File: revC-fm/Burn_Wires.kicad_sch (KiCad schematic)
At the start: 14 parts, among them Q19 MMBT2222AWT3G, Q20 DMN100-7-F, Q21 DMN100-7-F, Q22 IRF7404TRPBF, Q23 IRF7404TRPBF, U23 PE014006

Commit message: working revC
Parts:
- added J6 (x2): T1M-04-F-SV-L, mainboard-SLI:T1M-04-F-SV-L, symbol Connector_Generic:Conn_01x04
- Q19: value MMBT2222AWT3G -> MMBT2222LT1G; footprint Package_TO_SOT_SMD:SOT-323_SC-70 -> Package_TO_SOT_SMD:SOT-23-3
- Q20, Q21: value DMN100-7-F -> MMBT2222AWT3G; footprint mainboard:SOT-23 -> Package_TO_SOT_SMD:SOT-323_SC-70; symbol mainboard:IRLML2803TRPBF -> Device:Q_NPN_BEC; Flight DMN100-7-F -> (none)
- Q22, Q23: symbol mainboard:NDS8434 -> mainboard_SLI:IRF7404TRPBF; Flight IRF7404TRPBF -> (none)
- R167: value 4.7k -> 1k
- R168, R169: value 10k -> 1k
- R170, R171: value 4.7k -> 1Meg
- R172: value 100k -> 10Meg
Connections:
- net ENAB_BURN1: no longer R168.1
- net ENAB_BURN2: no longer R169.1
- net GND: now also J6.3 (Pin_3), J6.3 (Pin_3), J6.4 (Pin_4), J6.4 (Pin_4); no longer R168.2, R169.2
- net VBURN1: now also Q22.1 (S), Q22.2 (S), Q22.3 (S), J6.1 (Pin_1), J6.2 (Pin_2); no longer Q22.5 (Drain), Q22.6 (Drain), Q22.7 (Drain), Q22.8 (Drain)
- net VBURN2: now also J6.1 (Pin_1), J6.2 (Pin_2)
- net VBURN_A_IN: now also Q22.5 (D), Q22.6 (D), Q22.7 (D), Q22.8 (D); no longer Q22.1 (Source), Q22.2 (Source), Q22.3 (Source)
- net at Q20.3 (C), R172.1: now also R168.1; no longer Q22.4 (Gate)
- net at Q21.3 (C), R173.1: now also R169.1; no longer Q23.4 (Gate)
- new net: Q23.4 (G), R169.2
- new net: Q22.4 (G), R168.2
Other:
- note added: "in a larger package than other NPN's due to temp. derating"
- moved on the sheet: Q19, R167, R168, R169, R170, R171, R173

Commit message: working revC
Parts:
- Q20: renamed from Q22; value IRF7404TRPBF -> BSZ180P03NS3GATMA1; footprint Package_SO:SOIC-8_3.9x4.9mm_P1.27mm -> mainboard-SLI:PG-TSDSON-8_3.3x3.3mm; symbol mainboard_SLI:IRF7404TRPBF -> mainboard_SLI:BSZ180
- Q23: value IRF7404TRPBF -> BSZ180P03NS3GATMA1; footprint Package_SO:SOIC-8_3.9x4.9mm_P1.27mm -> mainboard-SLI:PG-TSDSON-8_3.3x3.3mm; symbol mainboard_SLI:IRF7404TRPBF -> mainboard_SLI:BSZ180
- renumbered D9 to D12, Q19 to Q21, Q20 to Q22, Q21 to Q24, R172 to R149, R168 to R150, R167 to R151, R170 to R152, R173 to R153, R169 to R154, R171 to R155, U23 to U20
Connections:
- net VBURN1: no longer Q20.2 (S), Q20.3 (S)
- net VBURN2: no longer Q23.6 (D), Q23.7 (D), Q23.8 (D)
- net VBURN_A_IN: no longer Q20.6 (D), Q20.7 (D), Q20.8 (D), Q23.2 (S), Q23.3 (S)

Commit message: working revC
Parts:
- removed D12: DFLS130L, mainboard:PWRDI-123, symbol mainboard:DFLS130L
- removed Q22, Q24: MMBT2222AWT3G, Package_TO_SOT_SMD:SOT-323_SC-70, symbol Device:Q_NPN_BEC
- added D9: SBRT5A50SA-13, Diode_SMD:D_SMA, symbol mainboard-rescue:D_Schottky-Device-mainboard-rescue
- added Q29 (x2): MMDT5551-7-F, Package_TO_SOT_SMD:SOT-363_SC-70-6, symbol Transistor_BJT:MMDT5551
- J6: footprint mainboard-SLI:T1M-04-F-SV-L -> SierraLobo:SAMTEC_T1M-04-F-SV-L
- K1: renamed from U20; footprint mainboard:RELAY_PE014006 -> SierraLobo:PE014006; symbol mainboard:PE014005 -> SierraLobo:PE014005; Flight PE014006 TE -> (none); Manufacturer_Name TE Connectivity -> (none); Manufacturer_Part_Number PE014006 TE -> (none); Proto TE Connectivity -> (none)
- Q38: renamed from Q20; footprint mainboard-SLI:PG-TSDSON-8_3.3x3.3mm -> SierraLobo:PG-TSDSON-8_3.3x3.3mm; symbol mainboard_SLI:BSZ180 -> SierraLobo:BSZ086
- Q41: renamed from Q23; footprint mainboard-SLI:PG-TSDSON-8_3.3x3.3mm -> SierraLobo:PG-TSDSON-8_3.3x3.3mm; symbol mainboard_SLI:BSZ180 -> SierraLobo:BSZ086
- R190: renamed from R149; value 10Meg -> 100k
- R193: renamed from R152; value 1Meg -> 100k
- R196: renamed from R155; value 1Meg -> 100k
- renumbered Q21 to Q39, R150 to R191, R151 to R192, R153 to R194, R154 to R195
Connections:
- net GND: now also Q29.4 (E2), Q29.4 (E2)
- net VBURN1: now also Q38.5 (D); no longer Q38.1 (S)
- net VBURN_A_IN: now also Q38.1 (S); no longer Q38.5 (D)
- net VBUS: now also D9.1 (K)
- net at R196.1: now also Q29.5 (B2)
- net at K1.5 (A2), Q39.3 (C): now also D9.2 (A)
- net at R194.1, R195.1: now also Q29.3 (C2)
- net at R190.1, R191.1: now also Q29.3 (C2)
- net at R193.1: now also Q29.5 (B2)
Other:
- moved on the sheet: J6, Q38

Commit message: routing fm
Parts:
- removed J6 (x2): T1M-04-F-SV-L, SierraLobo:SAMTEC_T1M-04-F-SV-L, symbol Connector_Generic:Conn_01x04
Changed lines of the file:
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@@
     (company "Sierra Lobo INC.")
   )
-  (junction (at 252.73 39.37) (diameter 0) (color 0 0 0 0)
-  )
   (junction (at 124.46 30.48) (diameter 0) (color 0 0 0 0)
   )
@@
   (junction (at 58.42 38.1) (diameter 0) (color 0 0 0 0)
   )
-  (junction (at 252.73 50.8) (diameter 0) (color 0 0 0 0)
-  )
   (junction (at 58.42 30.48) (diameter 0) (color 0 0 0 0)
   )
@@
   (junction (at 170.18 60.96) (diameter 0) (color 0 0 0 0)
   )
-  (junction (at 252.73 34.29) (diameter 0) (color 0 0 0 0)
-  )
-  (junction (at 252.73 55.88) (diameter 0) (color 0 0 0 0)
-  )
-  (wire (pts (xy 252.73 36.83) (xy 255.27 36.83))
-    (stroke (width 0) (type default))
-  )
   (wire (pts (xy 170.18 30.48) (xy 170.18 31.75))
     (stroke (width 0) (type default))
@@
     (stroke (width 0) (type default))
   )
-  (wire (pts (xy 252.73 50.8) (xy 255.27 50.8))
-    (stroke (width 0) (type default))
-  )
   (wire (pts (xy 144.78 48.26) (xy 154.94 48.26))
     (stroke (width 0) (type default))
@@
     (stroke (width 0) (type default))
   )
-  (wire (pts (xy 252.73 53.34) (xy 255.27 53.34))
-    (stroke (width 0) (type default))
-  )
   (wire (pts (xy 170.18 60.96) (xy 185.42 60.96))
     (stroke (width 0) (type default))
@@
     (stroke (width 0) (type default))
   )
-  (wire (pts (xy 255.27 31.75) (xy 252.73 31.75))
-    (stroke (width 0) (type default))
-  )
   (wire (pts (xy 170.18 69.85) (xy 170.18 73.025))
     (stroke (width 0) (type default))
@@
     (stroke (width 0) (type default))
   )
-  (wire (pts (xy 252.73 55.88) (xy 252.73 53.34))
-    (stroke (width 0) (type default))
-  )
-  (wire (pts (xy 252.73 31.75) (xy 252.73 34.29))
-    (stroke (width 0) (type default))
-  )
-  (wire (pts (xy 252.73 34.29) (xy 255.27 34.29))
-    (stroke (width 0) (type default))
-  )
   (wire (pts (xy 58.42 52.705) (xy 58.42 55.88))
     (stroke (width 0) (type default))
@@
     (stroke (width 0) (type default))
   )
-  (wire (pts (xy 252.73 39.37) (xy 252.73 36.83))
-    (stroke (width 0) (type default))
-  )
   (wire (pts (xy 124.46 30.48) (xy 170.18 30.48))
     (stroke (width 0) (type default))
   )
-  (wire (pts (xy 250.19 34.29) (xy 252.73 34.29))
-    (stroke (width 0) (type default))
-  )
   (wire (pts (xy 195.58 60.96) (xy 215.265 60.96))
     (stroke (width 0) (type default))
@@
     (stroke (width 0) (type default))
   )
-  (wire (pts (xy 255.27 39.37) (xy 252.73 39.37))
-    (stroke (width 0) (type default))
-  )
   (wire (pts (xy 124.46 60.96) (xy 170.18 60.96))
     (stroke (width 0) (type default))
@@
     (stroke (width 0) (type default))
   )
-  (wire (pts (xy 252.73 48.26) (xy 252.73 50.8))
-    (stroke (width 0) (type default))
-  )
   (wire (pts (xy 38.1 47.625) (xy 41.91 47.625))
     (stroke (width 0) (type default))
@@
     (stroke (width 0) (type default))
   )
-  (wire (pts (xy 250.19 50.8) (xy 252.73 50.8))
-    (stroke (width 0) (type default))
-  )
   (polyline (pts (xy 176.53 162.56) (xy 284.48 162.56))
     (stroke (width 0) (type default))
@@
     (stroke (width 0) (type default))
   )
-  (wire (pts (xy 255.27 48.26) (xy 252.73 48.26))
-    (stroke (width 0) (type default))
-  )
   (wire (pts (xy 58.42 38.1) (xy 63.5 38.1))
     (stroke (width 0) (type default))
   )
   (wire (pts (xy 49.53 47.625) (xy 50.8 47.625))
-    (stroke (width 0) (type default))
-  )
-  (wire (pts (xy 255.27 55.88) (xy 252.73 55.88))
     (stroke (width 0) (type default))
   )
@@
     )
   )
-  (global_label "VBURN1" (shape input) (at 215.265 30.48 0) (fields_autoplaced)
-    (effects (font (size 1.27 1.27) (thickness 0.254) bold) (justify left))
-    (property "Intersheetrefs" "${INTERSHEET_REFS}" (at 1.905 -5.08 0)
-      (effects (font (size 1.27 1.27)) hide)
+  (global_label "VBURN1" (shape output) (at 215.265 30.48 0) (fields_autoplaced)
+    (effects (font (size 1.27 1.27)) (justify left))
+    (property "Intersheetrefs" "${INTERSHEET_REFS}" (at 225.0157 30.48 0)
+      (effects (font (size 1.27 1.27)) (justify left) hide)
     )
   )
@@
     )
   )
-  (global_label "VBURN2" (shape input) (at 250.19 50.8 180) (fields_autoplaced)
-    (effects (font (size 1.27 1.27) (thickness 0.254) bold) (justify right))
-    (property "Intersheetrefs" "${INTERSHEET_REFS}" (at 463.55 -8.89 0)
-      (effects (font (size 1.27 1.27)) (justify left) hide)
-    )
-  )
-  (global_label "VBURN2" (shape input) (at 215.265 60.96 0) (fields_autoplaced)
-    (effects (font (size 1.27 1.27) (thickness 0.254) bold) (justify left))
-    (property "Intersheetrefs" "${INTERSHEET_REFS}" (at 1.905 1.27 0)
-      (effects (font (size 1.27 1.27)) hide)
-    )
-  )
-  (global_label "VBURN1" (shape input) (at 250.19 34.29 180) (fields_autoplaced)
-    (effects (font (size 1.27 1.27) (thickness 0.254) bold) (justify right))
-    (property "Intersheetrefs" "${INTERSHEET_REFS}" (at 463.55 -1.27 0)
+  (global_label "VBURN2" (shape output) (at 215.265 60.96 0) (fields_autoplaced)
+    (effects (font (size 1.27 1.27)) (justify left))
+    (property "Intersheetrefs" "${INTERSHEET_REFS}" (at 225.0157 60.96 0)
       (effects (font (size 1.27 1.27)) (justify left) hide)
     )
@@
     )
   )
-  (symbol (lib_id "power:GND") (at 252.73 39.37 0) (unit 1)
-    (in_bom yes) (on_board yes) (dnp no)
-    (property "Reference" "#PWR0122" (at 252.73 45.72 0)
-      (effects (font (size 1.27 1.27)) hide)
-    )
-    (property "Value" "GND" (at 252.73 43.18 0)
-      (effects (font (size 1.27 1.27)))
-    )
-    (property "Footprint" "" (at 252.73 39.37 0)
-      (effects (font (size 1.27 1.27)) hide)
-    )
-    (property "Datasheet" "" (at 252.73 39.37 0)
-      (effects (font (size 1.27 1.27)) hide)
-    )
-    (pin "1")
-    (instances
-      (project "mainboard"
-        (path "/d1441985-7b63-4bf8-a06d-c70da2e3b78b/00000000-0000-0000-0000-00005cec6476"
-          (reference "#PWR0122") (unit 1)
-        )
-      )
-    )
-  )
   (symbol (lib_id "Transistor_BJT:MMDT5551") (at 167.64 81.28 0) (unit 2)
     (in_bom yes) (on_board yes) (dnp no)
@@
     )
   )
-  (symbol (lib_id "power:GND") (at 252.73 55.88 0) (unit 1)
-    (in_bom yes) (on_board yes) (dnp no)
-    (property "Reference" "#PWR0125" (at 252.73 62.23 0)
-      (effects (font (size 1.27 1.27)) hide)
-    )
-    (property "Value" "GND" (at 252.73 59.69 0)
-      (effects (font (size 1.27 1.27)))
-    )
-    (property "Footprint" "" (at 252.73 55.88 0)
-      (effects (font (size 1.27 1.27)) hide)
-    )
-    (property "Datasheet" "" (at 252.73 55.88 0)
-      (effects (font (size 1.27 1.27)) hide)
-    )
-    (pin "1")
-    (instances
-      (project "mainboard"
-        (path "/d1441985-7b63-4bf8-a06d-c70da2e3b78b/00000000-0000-0000-0000-00005cec6476"
-          (reference "#PWR0125") (unit 1)
-        )
-      )
-    )
-  )
   (symbol (lib_id "Transistor_BJT:MMDT5551") (at 167.64 48.26 0) (unit 2)
     (in_bom yes) (on_board yes) (dnp no)
@@
         )
       )
-    )
-  )
-  (symbol (lib_id "Connector_Generic:Conn_01x04") (at 260.35 50.8 0) (unit 1)
-    (in_bom yes) (on_board yes) (dnp no) (fields_autoplaced)
-    (property "Reference" "J6" (at 262.89 50.7999 0)
-      (effects (font (size 1.27 1.27)) (justify left))
-    )
-    (property "Value" "T1M-04-F-SV-L" (at 262.89 53.3399 0)
-      (effects (font (size 1.27 1.27)) (justify left))
-    )
-    (property "Footprint" "SierraLobo:SAMTEC_T1M-04-F-SV-L" (at 260.35 50.8 0)
-      (effects (font (size 1.27 1.27)) hide)
-    )
-    (property "Datasheet" "~" (at 260.35 50.8 0)
-      (effects (font (size 1.27 1.27)) hide)
-    )
-    (pin "1")
-    (pin "2")
-    (pin "3")
-    (pin "4")
-    (instances
-      (project "mainboard"
-        (path "/d1441985-7b63-4bf8-a06d-c70da2e3b78b/00000000-0000-0000-0000-00005cec60eb"
-          (reference "J6") (unit 1)
-        )
-        (path "/d1441985-7b63-4bf8-a06d-c70da2e3b78b/00000000-0000-0000-0000-00005cec6476"
-          (reference "J5") (unit 1)
-        )
-      )
-    )
-  )
-  (symbol (lib_id "Connector_Generic:Conn_01x04") (at 260.35 34.29 0) (unit 1)
-    (in_bom yes) (on_board yes) (dnp no) (fields_autoplaced)
-    (property "Reference" "J6" (at 262.89 34.2899 0)
-      (effects (font (size 1.27 1.27)) (justify left))
-    )
-    (property "Value" "T1M-04-F-SV-L" (at 262.89 36.8299 0)
-      (effects (font (size 1.27 1.27)) (justify left))
-    )
-    (property "Footprint" "SierraLobo:SAMTEC_T1M-04-F-SV-L" (at 260.35 34.29 0)
-      (effects (font (size 1.27 1.27)) hide)
-    )
-    (property "Datasheet" "~" (at 260.35 34.29 0)
-      (effects (font (size 1.27 1.27)) hide)
-    )
-    (pin "1")
-    (pin "2")
-    (pin "3")
-    (pin "4")
-    (instances
-      (project "mainboard"
-        (path "/d1441985-7b63-4bf8-a06d-c70da2e3b78b/00000000-0000-0000-0000-00005cec60eb"
-          (reference "J6") (unit 1)
-        )
-        (path "/d1441985-7b63-4bf8-a06d-c70da2e3b78b/00000000-0000-0000-0000-00005cec6476"
-          (reference "J4") (unit 1)
-        )
-      )

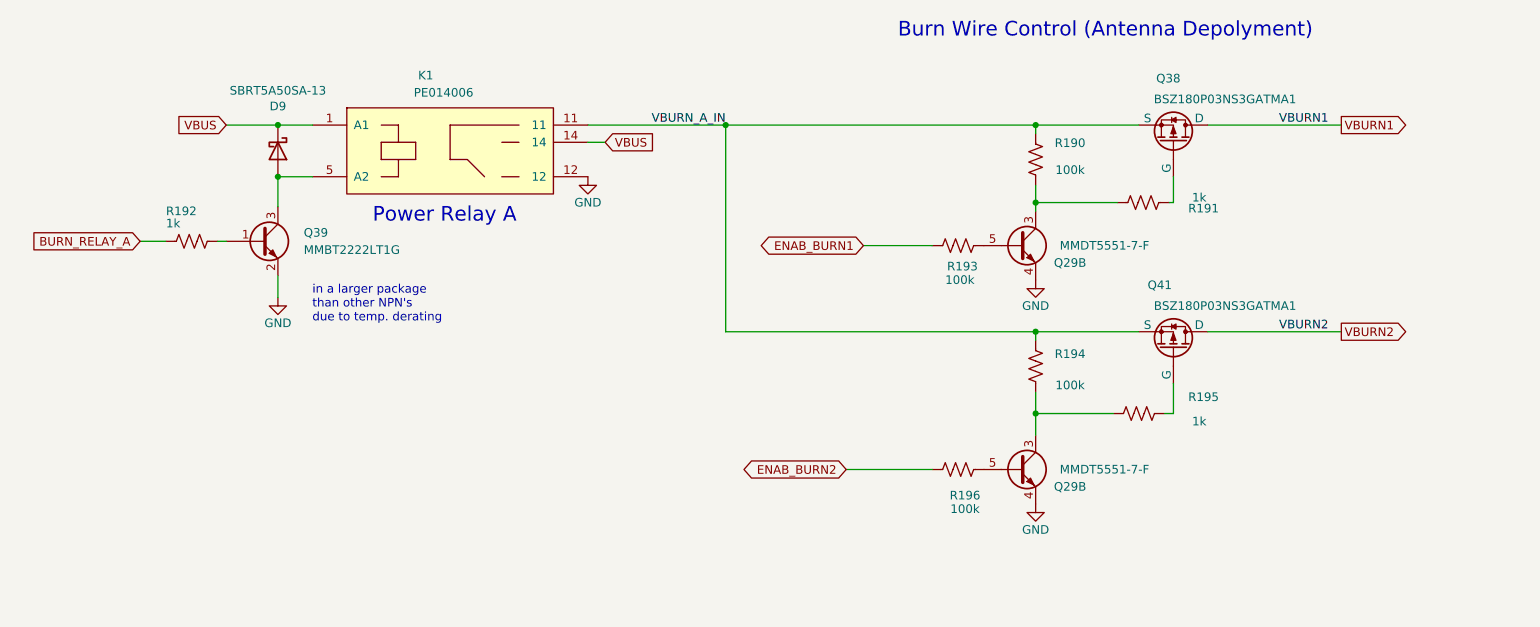
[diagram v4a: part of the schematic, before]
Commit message: updated analog , solar comp, layout
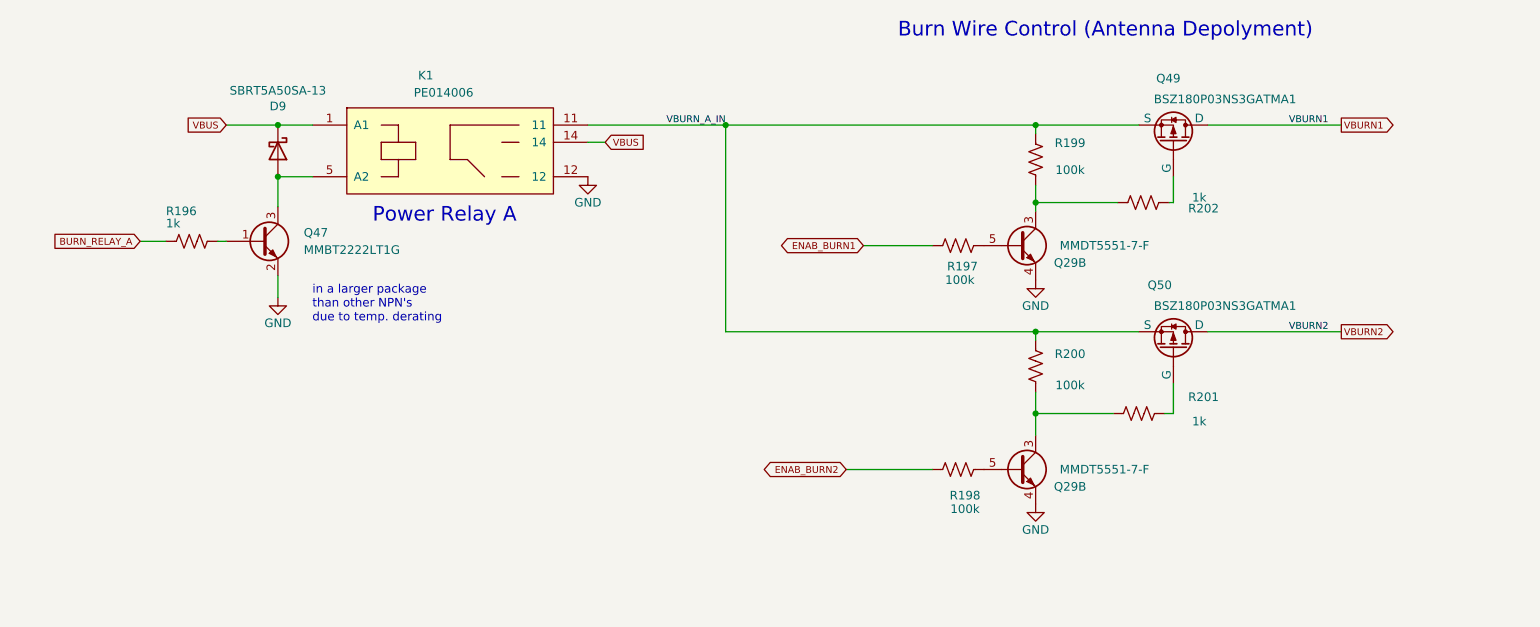
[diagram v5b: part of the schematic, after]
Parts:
- renumbered Q39 to Q47, Q38 to Q49, Q41 to Q50, R192 to R196, R193 to R197, R196 to R198, R190 to R199, R194 to R200, R195 to R201, R191 to R202
